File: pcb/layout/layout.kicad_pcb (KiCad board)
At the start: 2 copper layers, 28 x 70 mm, 15 parts, among them J1 B2B-PH-K-S, J2 BM02B-SRSS-TB(LF)(SN), SW1 PTS841GKSMTR LFS, SW2 JS202011AQN, U1 113991115, U2 MAX98357AETE+T

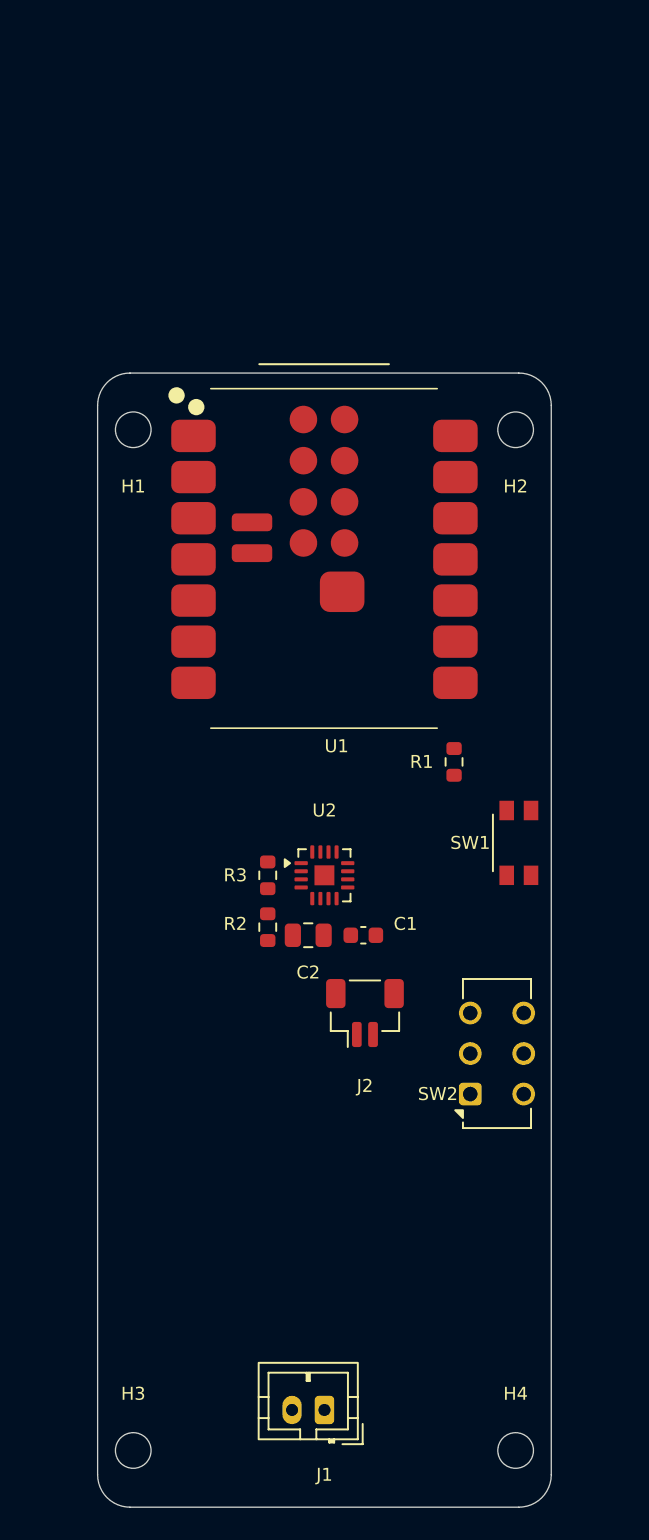
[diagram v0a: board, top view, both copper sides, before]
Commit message: Add comprehensive BOM, redesign docs, and updated CAD files
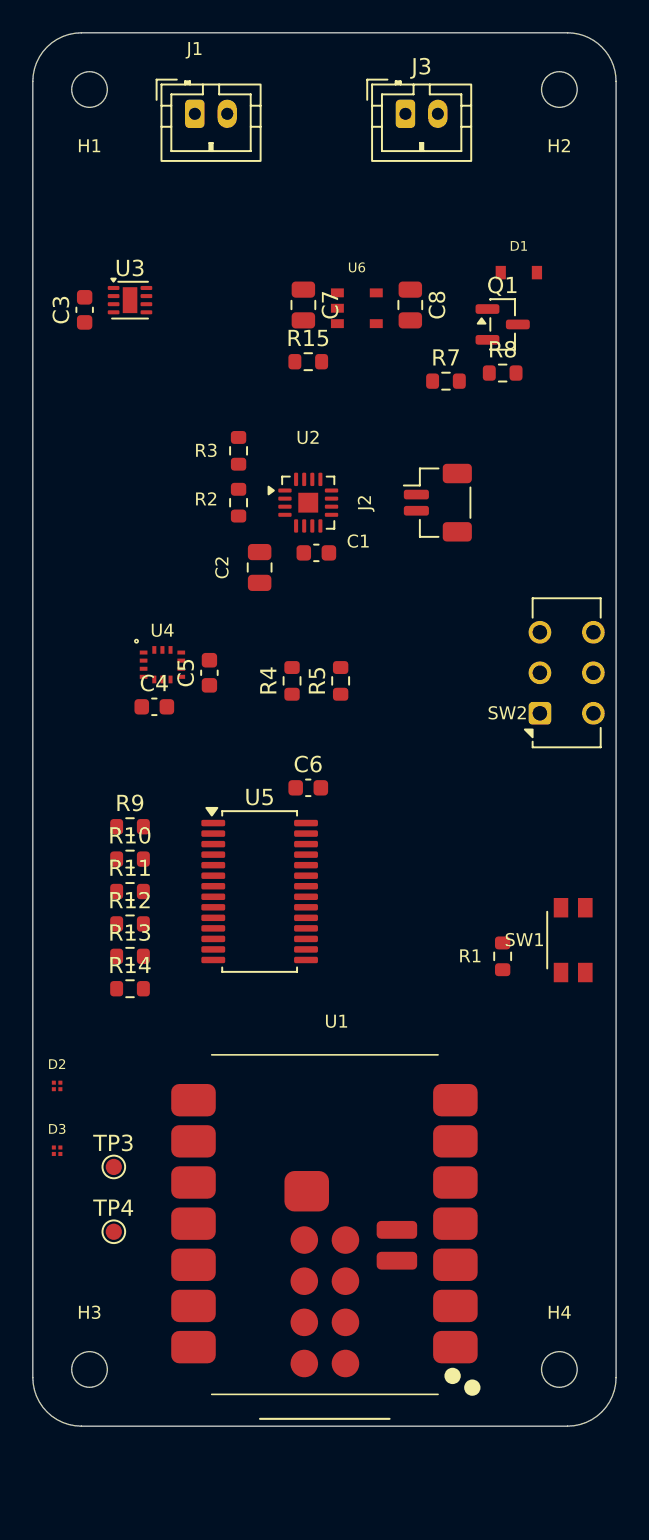
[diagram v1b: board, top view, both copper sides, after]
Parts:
- added C3: GCM188R71H104KA57J, stdlib_kicad-footprints_Capacitor_SMD:C_0603_1608Metric, F.Cu at (85.2, 61.1)
- added C4: GCM188R71H104KA57J, stdlib_kicad-footprints_Capacitor_SMD:C_0603_1608Metric, F.Cu at (89.5, 85.6)
- added C5: GCM188R71H104KA57J, stdlib_kicad-footprints_Capacitor_SMD:C_0603_1608Metric, F.Cu at (92.9, 83.5)
- added C6: GCM188R71H104KA57J, stdlib_kicad-footprints_Capacitor_SMD:C_0603_1608Metric, F.Cu at (99.0, 90.6)
- added C7: CC0805KRX5R8BB106, stdlib_kicad-footprints_Capacitor_SMD:C_0805_2012Metric, F.Cu at (98.7, 60.8)
- added C8: CC0805KRX5R8BB106, stdlib_kicad-footprints_Capacitor_SMD:C_0805_2012Metric, F.Cu at (105.3, 60.8)
- added D1: NSVR0320MW2T1G, embedr_ai_pendant_recorder_components_motor-diode:NSVR0320, F.Cu at (112.0, 58.8)
- added D2: APGF0607G32B33R23-05, embedr_ai_pendant_recorder_components_rgb:APGF0607, F.Cu at (83.5, 109.0)
- added D3: APGF0607G32B33R23-05, embedr_ai_pendant_recorder_components_rgb:APGF0607, F.Cu at (83.5, 113.0)
- added J3: B2B-PH-K-S, embedr_ai_pendant_recorder_components_jst-b2b-ph-k-s_assets:JST_PH_B2B-PH-K_1x02_P2.00mm_Vertical, F.Cu at (105.0, 49.0)
- added Q1: AO3400A, embedr_ai_pendant_recorder_components_ao3400a_assets:SOT-23, F.Cu at (111.0, 62.0)
- added R10: RC0603FR-072KL, stdlib_kicad-footprints_Resistor_SMD:R_0603_1608Metric, F.Cu at (88.0, 95.0)
- added R11: RC0603FR-072KL, stdlib_kicad-footprints_Resistor_SMD:R_0603_1608Metric, F.Cu at (88.0, 97.0)
- added R12: RC0603FR-072KL, stdlib_kicad-footprints_Resistor_SMD:R_0603_1608Metric, F.Cu at (88.0, 99.0)
- added R13: RC0603FR-072KL, stdlib_kicad-footprints_Resistor_SMD:R_0603_1608Metric, F.Cu at (88.0, 101.0)
- added R14: RC0603FR-072KL, stdlib_kicad-footprints_Resistor_SMD:R_0603_1608Metric, F.Cu at (88.0, 103.0)
- added R15: RC0603FR-07100KL, stdlib_kicad-footprints_Resistor_SMD:R_0603_1608Metric, F.Cu at (99.0, 64.3)
- added R4: RC0603FR-074K7L, stdlib_kicad-footprints_Resistor_SMD:R_0603_1608Metric, F.Cu at (98.0, 84.0)
- added R5: RC0603FR-074K7L, stdlib_kicad-footprints_Resistor_SMD:R_0603_1608Metric, F.Cu at (101.0, 84.0)
- added R7: RC0603FR-07100RL, stdlib_kicad-footprints_Resistor_SMD:R_0603_1608Metric, F.Cu at (107.5, 65.5)
- added R8: RC0603FR-07100KL, stdlib_kicad-footprints_Resistor_SMD:R_0603_1608Metric, F.Cu at (111.0, 65.0)
- added R9: RC0603FR-072KL, stdlib_kicad-footprints_Resistor_SMD:R_0603_1608Metric, F.Cu at (88.0, 93.0)
- added TP3: ?, stdlib_kicad-footprints_TestPoint:TestPoint_Pad_D1.0mm, F.Cu at (87.0, 114.0)
- added TP4: ?, stdlib_kicad-footprints_TestPoint:TestPoint_Pad_D1.0mm, F.Cu at (87.0, 118.0)
- added U3: MAX17048G+T10, embedr_ai_pendant_recorder_components_max17048g-t10_assets:kicad_footprint, F.Cu at (88.0, 60.5)
- added U4: BMI270, embedr_ai_pendant_recorder_components_bmi270:BMI270, F.Cu at (90.0, 83.0)
- added U5: PCA9685PW,118, embedr_ai_pendant_recorder_components_pca9685pw_assets:TSSOP-28_4.4x9.7mm_P0.65mm, F.Cu at (96.0, 97.0)
- added U6: AP2112K-3.3TRG1, embedr_ai_pendant_recorder_components_motor-ldo:AP2112K_3V3, F.Cu at (102.0, 61.0)
- C1: value 100nF 6.3V -> GCM188R71H104KA57J
- C2: value 10uF 6.3V -> CC0805KRX5R8BB106
- R1, R2: value 100k -> RC0603FR-07100KL
- R3: value 2k -> RC0603FR-072KL
- moved J1 80.4 mm to (92.0, 49.0), turned to 0 degrees
- moved J2 31.8 mm to (107.0, 73.0), turned to 270 degrees
- moved U1 26.8 mm to (108.9, 107.0), turned to 180 degrees
- moved R2 26.3 mm to (94.7, 73.0)
- moved R3 26.3 mm to (94.7, 69.8)
- moved SW2 23.9 mm to (113.3, 86.0)
- moved C1 23.8 mm to (99.5, 76.1)
- moved U2 23.0 mm to (99.0, 73.0)
- moved C2 22.9 mm to (96.0, 77.0), turned to 270 degrees
- moved H1 21.2 mm to (85.5, 47.5)
- moved H2 21.2 mm to (114.5, 47.5)
- moved R1 12.4 mm to (111.0, 101.0)
- moved SW1 6.87 mm to (115.3, 100.0)
- moved H3 5.68 mm to (85.5, 126.5)
- moved H4 5.68 mm to (114.5, 126.5)
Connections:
- U1 pad 1: U1.D0 -> HAPTIC_ARM
- U1 pad 3: U1.D2 -> AMP_ENABLE
- U1 pad 5: AMP_ENABLE -> FG_SDA
- U1 pad 6: U1.D5_SCL -> FG_SCL
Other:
- board size 28 x 70 mm -> 36 x 86 mm
